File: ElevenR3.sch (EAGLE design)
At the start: 63 parts, among them IC1 ATMEGA328P, IC2 ATMEGA16U2-MU, IC3 MC33269DT-5.0, IC4 LM358D, IC5 LP2985-33DBVR, J2 Analog, J3 Digital_8_13, J4 Digital_0_7, J5 DC_2_1MM, J6 Digital_0_7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

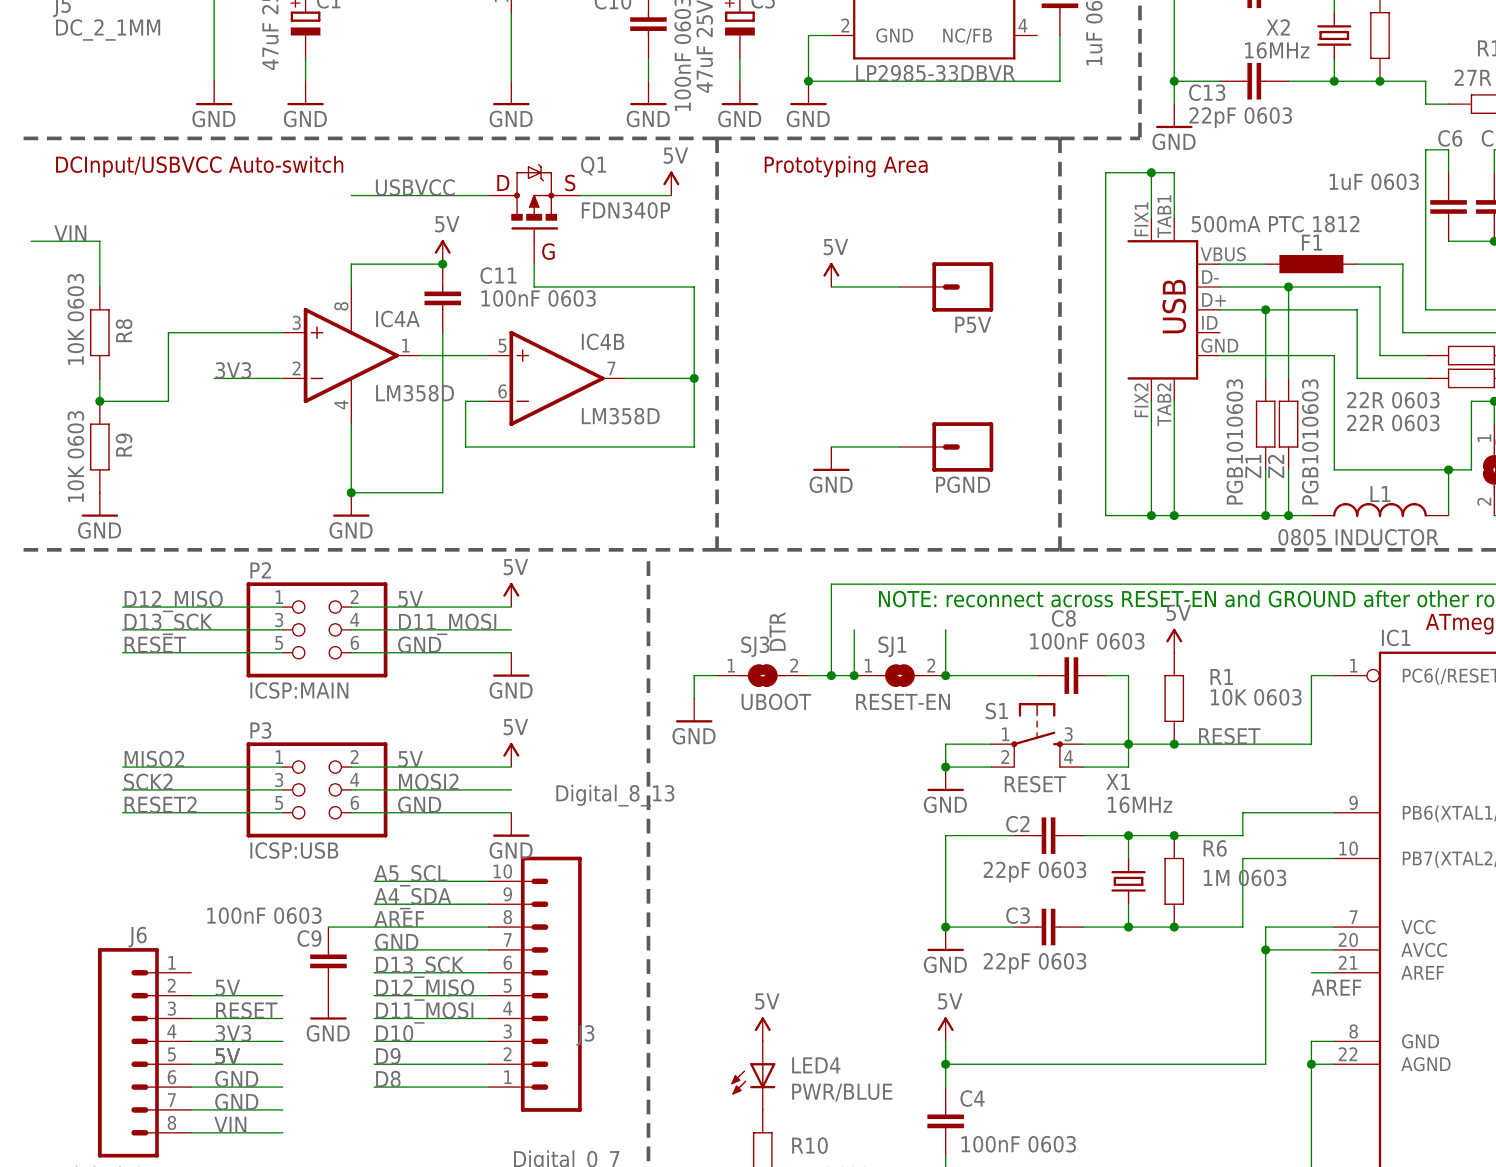
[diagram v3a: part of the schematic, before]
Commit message: Replaced uUSB footprint
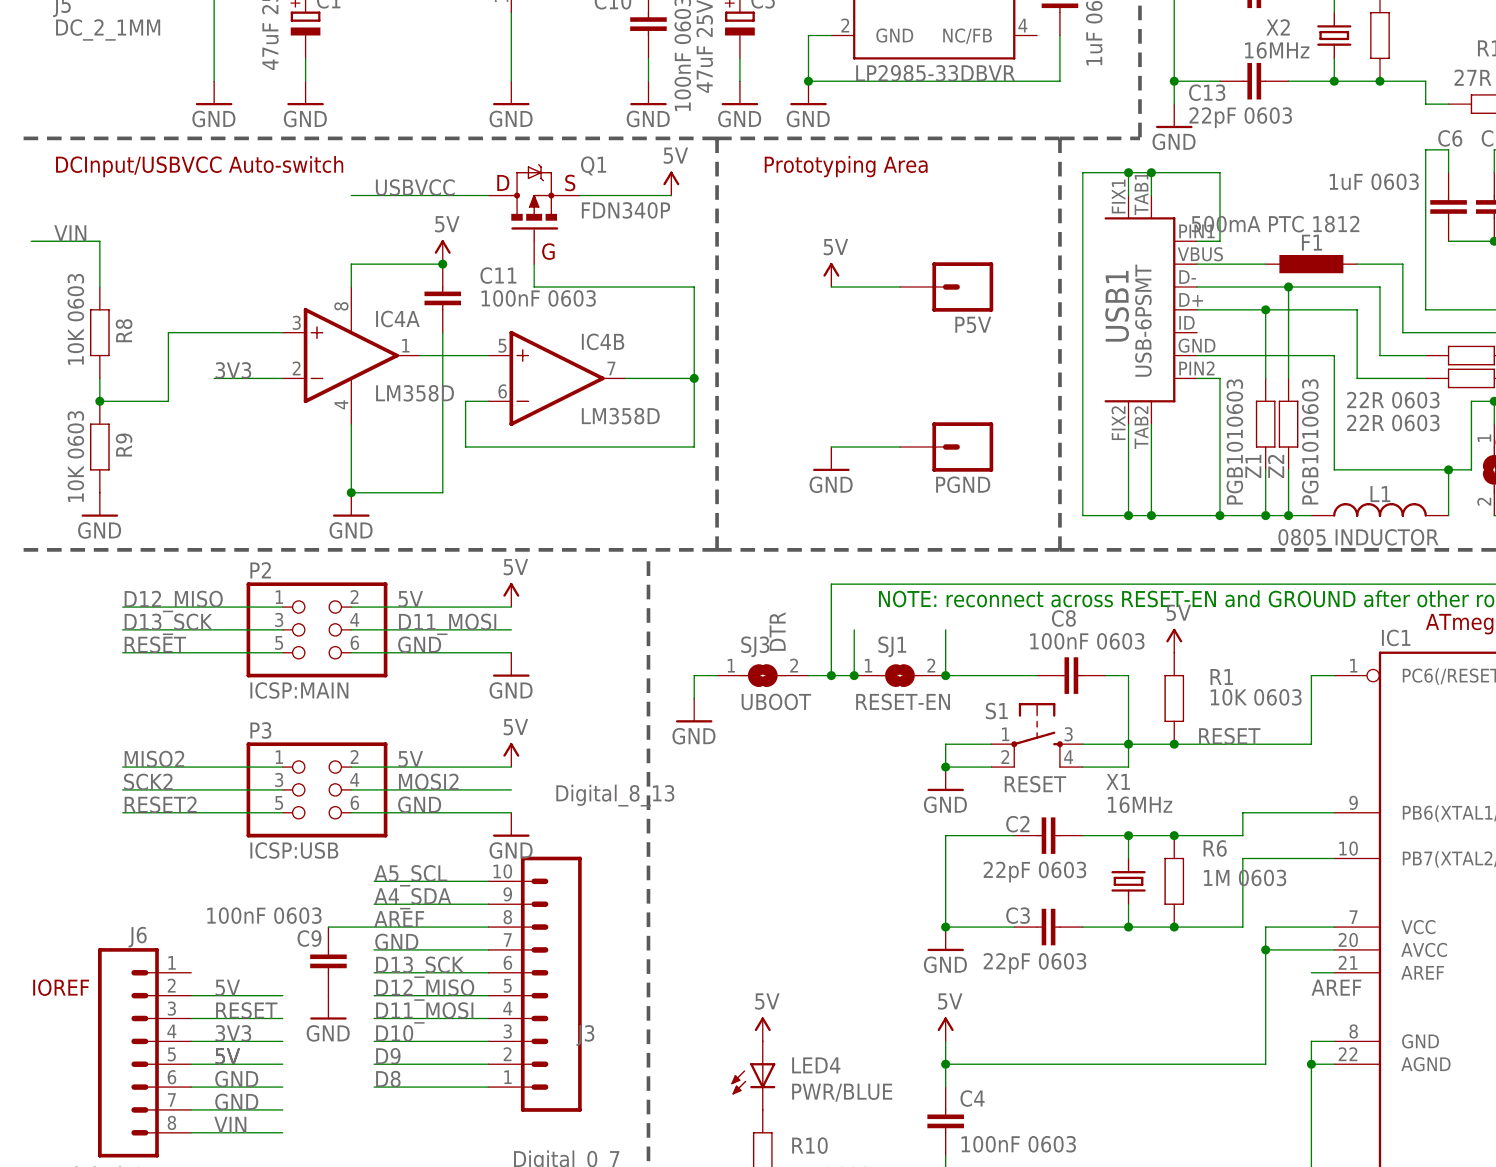
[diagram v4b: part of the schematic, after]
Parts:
- removed X3: USBSF-MICROB, freetronics-jon:USBSF-MICROB
- added USB1: USB-6PSMT, freetronics-jon:USB-6PSMT
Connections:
- net N$115: now also USB1.VBUS; no longer X3.VBUS
- net N$16: now also USB1.D+; no longer X3.D+
- net N$17: now also USB1.D-; no longer X3.D-
- net N$3: now also USB1.FIX1, USB1.FIX2, USB1.PIN1, USB1.PIN2, USB1.TAB1, USB1.TAB2; no longer X3.FIX1, X3.FIX2, X3.TAB1, X3.TAB2
- net UGND: now also USB1.GND; no longer X3.GND
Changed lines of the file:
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@@
 <part name="GND6" library="SparkFun" deviceset="GND" device=""/>
 <part name="J6" library="freetronics" deviceset="M08" device="" value="Digital_0_7"/>
-<part name="X3" library="freetronics-jon" deviceset="USBSF" device="-MICROB"/>
+<part name="USB1" library="freetronics-jon" deviceset="USB-6P" device="SMT"/>
 </parts>
 <sheets>
@@
 <frame x1="142.24" y1="5.08" x2="243.84" y2="17.78" columns="0" rows="0" layer="94" border-left="no" border-top="no" border-right="no" border-bottom="no"/>
 <text x="167.64" y="111.76" size="1.27" layer="94">(Linked)</text>
+<text x="5.08" y="50.8" size="1.778" layer="94">IOREF</text>
 </plain>
 <instances>
@@
 <attribute name="VALUE" x="8.128" y="31.75" size="1.778" layer="96" rot="MR180"/>
 </instance>
-<instance part="X3" gate="G$1" x="132.08" y="127" rot="R180"/>
+<instance part="USB1" gate="G$1" x="129.54" y="127" smashed="yes" rot="R180">
+<attribute name="NAME" x="127" y="123.19" size="2.54" layer="95" rot="R90"/>
+<attribute name="VALUE" x="129.54" y="119.38" size="1.778" layer="96" rot="R90"/>
+</instance>
 </instances>
 <busses>
@@
 <pinref part="Z2" gate="G$1" pin="2"/>
 <pinref part="L1" gate="G$1" pin="1"/>
-<pinref part="X3" gate="G$1" pin="TAB2"/>
-<wire x1="132.08" y1="116.84" x2="132.08" y2="104.14" width="0.1524" layer="91"/>
-<wire x1="132.08" y1="104.14" x2="142.24" y2="104.14" width="0.1524" layer="91"/>
-<pinref part="X3" gate="G$1" pin="TAB1"/>
-<wire x1="132.08" y1="137.16" x2="132.08" y2="142.24" width="0.1524" layer="91"/>
-<wire x1="132.08" y1="142.24" x2="129.54" y2="142.24" width="0.1524" layer="91"/>
-<wire x1="129.54" y1="142.24" x2="124.46" y2="142.24" width="0.1524" layer="91"/>
-<wire x1="124.46" y1="142.24" x2="124.46" y2="104.14" width="0.1524" layer="91"/>
-<wire x1="124.46" y1="104.14" x2="129.54" y2="104.14" width="0.1524" layer="91"/>
-<junction x="132.08" y="104.14"/>
-<pinref part="X3" gate="G$1" pin="FIX1"/>
-<wire x1="129.54" y1="104.14" x2="132.08" y2="104.14" width="0.1524" layer="91"/>
-<wire x1="129.54" y1="137.16" x2="129.54" y2="142.24" width="0.1524" layer="91"/>
-<pinref part="X3" gate="G$1" pin="FIX2"/>
-<wire x1="129.54" y1="116.84" x2="129.54" y2="104.14" width="0.1524" layer="91"/>
+<pinref part="USB1" gate="G$1" pin="TAB2"/>
+<wire x1="129.54" y1="114.3" x2="129.54" y2="104.14" width="0.1524" layer="91"/>
+<wire x1="129.54" y1="104.14" x2="137.16" y2="104.14" width="0.1524" layer="91"/>
+<pinref part="USB1" gate="G$1" pin="TAB1"/>
+<wire x1="137.16" y1="104.14" x2="142.24" y2="104.14" width="0.1524" layer="91"/>
+<wire x1="129.54" y1="139.7" x2="129.54" y2="142.24" width="0.1524" layer="91"/>
+<wire x1="129.54" y1="142.24" x2="127" y2="142.24" width="0.1524" layer="91"/>
+<wire x1="127" y1="142.24" x2="121.92" y2="142.24" width="0.1524" layer="91"/>
+<wire x1="121.92" y1="142.24" x2="121.92" y2="104.14" width="0.1524" layer="91"/>
+<wire x1="121.92" y1="104.14" x2="127" y2="104.14" width="0.1524" layer="91"/>
 <junction x="129.54" y="104.14"/>
+<pinref part="USB1" gate="G$1" pin="FIX1"/>
+<wire x1="127" y1="104.14" x2="129.54" y2="104.14" width="0.1524" layer="91"/>
+<wire x1="127" y1="139.7" x2="127" y2="142.24" width="0.1524" layer="91"/>
+<pinref part="USB1" gate="G$1" pin="FIX2"/>
+<wire x1="127" y1="114.3" x2="127" y2="104.14" width="0.1524" layer="91"/>
+<wire x1="129.54" y1="142.24" x2="137.16" y2="142.24" width="0.1524" layer="91"/>
+<wire x1="137.16" y1="142.24" x2="137.16" y2="134.62" width="0.1524" layer="91"/>
+<pinref part="USB1" gate="G$1" pin="PIN1"/>
+<wire x1="137.16" y1="134.62" x2="134.62" y2="134.62" width="0.1524" layer="91"/>
+<pinref part="USB1" gate="G$1" pin="PIN2"/>
+<wire x1="134.62" y1="119.38" x2="137.16" y2="119.38" width="0.1524" layer="91"/>
+<wire x1="137.16" y1="119.38" x2="137.16" y2="104.14" width="0.1524" layer="91"/>
+<junction x="127" y="104.14"/>
+<junction x="137.16" y="104.14"/>
 <junction x="129.54" y="142.24"/>
+<junction x="127" y="142.24"/>
 </segment>
 </net>
@@
 <pinref part="Z1" gate="G$1" pin="1"/>
 <pinref part="R15" gate="G$1" pin="2"/>
-<pinref part="X3" gate="G$1" pin="D+"/>
-<wire x1="142.24" y1="127" x2="137.16" y2="127" width="0.1524" layer="91"/>
+<pinref part="USB1" gate="G$1" pin="D+"/>
+<wire x1="142.24" y1="127" x2="134.62" y2="127" width="0.1524" layer="91"/>
 </segment>
 </net>
@@
 <pinref part="Z2" gate="G$1" pin="1"/>
 <pinref part="R14" gate="G$1" pin="2"/>
-<pinref part="X3" gate="G$1" pin="D-"/>
-<wire x1="137.16" y1="129.54" x2="144.78" y2="129.54" width="0.1524" layer="91"/>
+<pinref part="USB1" gate="G$1" pin="D-"/>
+<wire x1="134.62" y1="129.54" x2="144.78" y2="129.54" width="0.1524" layer="91"/>
 </segment>
 </net>
@@
 <segment>
 <pinref part="F1" gate="G$1" pin="1"/>
-<pinref part="X3" gate="G$1" pin="VBUS"/>
-<wire x1="142.24" y1="132.08" x2="137.16" y2="132.08" width="0.1524" layer="91"/>
+<pinref part="USB1" gate="G$1" pin="VBUS"/>
+<wire x1="142.24" y1="132.08" x2="134.62" y2="132.08" width="0.1524" layer="91"/>
 </segment>
 </net>
@@
 <net name="UGND" class="0">
 <segment>
-<wire x1="137.16" y1="121.92" x2="149.86" y2="121.92" width="0.1524" layer="91"/>
+<wire x1="134.62" y1="121.92" x2="149.86" y2="121.92" width="0.1524" layer="91"/>
 <wire x1="149.86" y1="121.92" x2="149.86" y2="109.22" width="0.1524" layer="91"/>
 <wire x1="149.86" y1="109.22" x2="162.56" y2="109.22" width="0.1524" layer="91"/>
@@
 <pinref part="IC2" gate="G$1" pin="UGND"/>
 <pinref part="SJ2" gate="1" pin="1"/>
-<pinref part="X3" gate="G$1" pin="GND"/>
+<pinref part="USB1" gate="G$1" pin="GND"/>
 <wire x1="170.18" y1="116.84" x2="170.18" y2="114.3" width="0.1524" layer="91"/>
 <junction x="170.18" y="116.84"/>

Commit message: Production release v2.0 after small revisions
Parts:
- J1: value Digital_0_7 -> Power
- LED1: value RX -> RX/GRN
- LED2: value TX -> TX/YEL
- renumbered J6 to J1, USB1 to P1
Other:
- note removed: "SCL/SDA"
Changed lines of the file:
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@@
 <part name="R2" library="freetronics" deviceset="RESISTOR" device="0603" value="1K 0603"/>
 <part name="R3" library="freetronics" deviceset="RESISTOR" device="0603" value="1K 0603"/>
-<part name="LED1" library="freetronics" deviceset="LED" device="0603" value="RX"/>
-<part name="LED2" library="freetronics" deviceset="LED" device="0603" value="TX"/>
+<part name="LED1" library="freetronics" deviceset="LED" device="0603" value="RX/GRN"/>
+<part name="LED2" library="freetronics" deviceset="LED" device="0603" value="TX/YEL"/>
 <part name="U$2" library="SparkFun" deviceset="5V" device=""/>
 <part name="R4" library="freetronics" deviceset="RESISTOR" device="0603" value="1K 0603"/>
@@
 <part name="GND1" library="SparkFun" deviceset="GND" device=""/>
 <part name="GND6" library="SparkFun" deviceset="GND" device=""/>
-<part name="J6" library="freetronics" deviceset="M08" device="" value="Digital_0_7"/>
-<part name="USB1" library="freetronics-jon" deviceset="USB-6P" device="SMT"/>
+<part name="J1" library="freetronics" deviceset="M08" device="" value="Power"/>
+<part name="P1" library="freetronics-jon" deviceset="USB-6P" device="SMT"/>
 </parts>
 <sheets>
@@
 <frame x1="0" y1="0" x2="248.92" y2="185.42" columns="8" rows="5" layer="94"/>
 <frame x1="83.82" y1="101.6" x2="116.84" y2="139.7" columns="0" rows="0" layer="94"/>
-<text x="254" y="160.02" size="1.778" layer="91">IOREF</text>
-<text x="254" y="154.94" size="1.778" layer="91">SCL/SDA</text>
 <text x="144.78" y="20.32" size="3.048" layer="94">Freetronics "Eleven" R3</text>
 <text x="170.18" y="14.478" size="1.778" layer="94">V3.0 (2012-07-02)</text>
@@
 <instance part="J3" gate="G$1" x="66.04" y="58.42" smashed="yes" rot="MR0">
 <attribute name="NAME" x="67.818" y="45.72" size="1.778" layer="95" rot="MR0"/>
-<attribute name="VALUE" x="76.708" y="72.39" size="1.778" layer="96" rot="MR0"/>
+<attribute name="VALUE" x="71.628" y="35.56" size="1.778" layer="96" rot="MR0"/>
 </instance>
 <instance part="J4" gate="G$1" x="60.96" y="17.78" smashed="yes" rot="MR0">
@@
 <instance part="F1" gate="G$1" x="147.32" y="132.08" smashed="yes" rot="R90">
 <attribute name="NAME" x="146.05" y="133.5786" size="1.778" layer="95"/>
-<attribute name="VALUE" x="133.858" y="135.636" size="1.778" layer="96"/>
+<attribute name="VALUE" x="138.938" y="135.636" size="1.778" layer="96"/>
 </instance>
 <instance part="R2" gate="G$1" x="241.3" y="129.54" smashed="yes" rot="R90">
@@
 <instance part="LED1" gate="G$1" x="241.3" y="142.24" smashed="yes">
 <attribute name="NAME" x="239.776" y="132.588" size="1.778" layer="95" rot="R90"/>
-<attribute name="VALUE" x="239.649" y="143.256" size="1.778" layer="96" rot="R90"/>
+<attribute name="VALUE" x="237.109" y="140.716" size="1.778" layer="96" rot="R90"/>
 </instance>
 <instance part="LED2" gate="G$1" x="233.68" y="142.24" smashed="yes">
 <attribute name="NAME" x="232.156" y="132.588" size="1.778" layer="95" rot="R90"/>
-<attribute name="VALUE" x="232.029" y="143.256" size="1.778" layer="96" rot="R90"/>
+<attribute name="VALUE" x="229.489" y="140.716" size="1.778" layer="96" rot="R90"/>
 </instance>
 <instance part="U$2" gate="G$1" x="241.3" y="147.32"/>
@@
 <attribute name="VALUE" x="180.34" y="101.6" size="1.778" layer="96"/>
 </instance>
-<instance part="J6" gate="G$1" x="17.78" y="45.72" smashed="yes" rot="MR180">
+<instance part="J1" gate="G$1" x="17.78" y="45.72" smashed="yes" rot="MR180">
 <attribute name="NAME" x="16.002" y="58.42" size="1.778" layer="95" rot="MR180"/>
-<attribute name="VALUE" x="8.128" y="31.75" size="1.778" layer="96" rot="MR180"/>
-</instance>
-<instance part="USB1" gate="G$1" x="129.54" y="127" smashed="yes" rot="R180">
+<attribute name="VALUE" x="12.446" y="32.004" size="1.778" layer="96" rot="MR180"/>
+</instance>
+<instance part="P1" gate="G$1" x="129.54" y="127" smashed="yes" rot="R180">
 <attribute name="NAME" x="127" y="123.19" size="2.54" layer="95" rot="R90"/>
 <attribute name="VALUE" x="129.54" y="119.38" size="1.778" layer="96" rot="R90"/>
@@
 <segment>
 <label x="25.4" y="45.72" size="1.778" layer="95"/>
-<pinref part="J6" gate="G$1" pin="4"/>
+<pinref part="J1" gate="G$1" pin="4"/>
 <wire x1="22.86" y1="45.72" x2="33.02" y2="45.72" width="0.1524" layer="91"/>
 </segment>
@@
 <label x="25.4" y="43.18" size="1.778" layer="95"/>
 <label x="25.4" y="43.18" size="1.778" layer="95"/>
-<pinref part="J6" gate="G$1" pin="5"/>
+<pinref part="J1" gate="G$1" pin="5"/>
 <wire x1="22.86" y1="43.18" x2="33.02" y2="43.18" width="0.1524" layer="91"/>
 </segment>
@@
 </segment>
 <segment>
-<pinref part="J6" gate="G$1" pin="2"/>
+<pinref part="J1" gate="G$1" pin="2"/>
 <wire x1="22.86" y1="50.8" x2="33.02" y2="50.8" width="0.1524" layer="91"/>
 <label x="25.4" y="50.8" size="1.778" layer="95"/>
@@
 <segment>
 <label x="25.4" y="40.64" size="1.778" layer="95"/>
-<pinref part="J6" gate="G$1" pin="6"/>
+<pinref part="J1" gate="G$1" pin="6"/>
 <wire x1="33.02" y1="40.64" x2="22.86" y2="40.64" width="0.1524" layer="91"/>
 </segment>
 <segment>
 <label x="25.4" y="38.1" size="1.778" layer="95"/>
-<pinref part="J6" gate="G$1" pin="7"/>
+<pinref part="J1" gate="G$1" pin="7"/>
 <wire x1="22.86" y1="38.1" x2="33.02" y2="38.1" width="0.1524" layer="91"/>
 </segment>
@@
 <segment>
 <label x="25.4" y="35.56" size="1.778" layer="95"/>
-<pinref part="J6" gate="G$1" pin="8"/>
+<pinref part="J1" gate="G$1" pin="8"/>
 <wire x1="33.02" y1="35.56" x2="22.86" y2="35.56" width="0.1524" layer="91"/>
 </segment>
@@
 <label x="134.62" y="78.74" size="1.778" layer="95"/>
 <label x="15.24" y="88.9" size="1.778" layer="95"/>
-<pinref part="J6" gate="G$1" pin="3"/>
+<pinref part="J1" gate="G$1" pin="3"/>
 <wire x1="33.02" y1="48.26" x2="22.86" y2="48.26" width="0.1524" layer="91"/>
 </segment>
@@
 <pinref part="Z2" gate="G$1" pin="2"/>
 <pinref part="L1" gate="G$1" pin="1"/>
-<pinref part="USB1" gate="G$1" pin="TAB2"/>
+<pinref part="P1" gate="G$1" pin="TAB2"/>
 <wire x1="129.54" y1="114.3" x2="129.54" y2="104.14" width="0.1524" layer="91"/>
 <wire x1="129.54" y1="104.14" x2="137.16" y2="104.14" width="0.1524" layer="91"/>
-<pinref part="USB1" gate="G$1" pin="TAB1"/>
+<pinref part="P1" gate="G$1" pin="TAB1"/>
 <wire x1="137.16" y1="104.14" x2="142.24" y2="104.14" width="0.1524" layer="91"/>
 <wire x1="129.54" y1="139.7" x2="129.54" y2="142.24" width="0.1524" layer="91"/>
@@
 <wire x1="121.92" y1="104.14" x2="127" y2="104.14" width="0.1524" layer="91"/>
 <junction x="129.54" y="104.14"/>
-<pinref part="USB1" gate="G$1" pin="FIX1"/>
+<pinref part="P1" gate="G$1" pin="FIX1"/>
 <wire x1="127" y1="104.14" x2="129.54" y2="104.14" width="0.1524" layer="91"/>
 <wire x1="127" y1="139.7" x2="127" y2="142.24" width="0.1524" layer="91"/>
-<pinref part="USB1" gate="G$1" pin="FIX2"/>
+<pinref part="P1" gate="G$1" pin="FIX2"/>
 <wire x1="127" y1="114.3" x2="127" y2="104.14" width="0.1524" layer="91"/>
 <wire x1="129.54" y1="142.24" x2="137.16" y2="142.24" width="0.1524" layer="91"/>
 <wire x1="137.16" y1="142.24" x2="137.16" y2="134.62" width="0.1524" layer="91"/>
-<pinref part="USB1" gate="G$1" pin="PIN1"/>
+<pinref part="P1" gate="G$1" pin="PIN1"/>
 <wire x1="137.16" y1="134.62" x2="134.62" y2="134.62" width="0.1524" layer="91"/>
-<pinref part="USB1" gate="G$1" pin="PIN2"/>
+<pinref part="P1" gate="G$1" pin="PIN2"/>
 <wire x1="134.62" y1="119.38" x2="137.16" y2="119.38" width="0.1524" layer="91"/>
 <wire x1="137.16" y1="119.38" x2="137.16" y2="104.14" width="0.1524" layer="91"/>
@@
 <pinref part="Z1" gate="G$1" pin="1"/>
 <pinref part="R15" gate="G$1" pin="2"/>
-<pinref part="USB1" gate="G$1" pin="D+"/>
+<pinref part="P1" gate="G$1" pin="D+"/>
 <wire x1="142.24" y1="127" x2="134.62" y2="127" width="0.1524" layer="91"/>
 </segment>
@@
 <pinref part="Z2" gate="G$1" pin="1"/>
 <pinref part="R14" gate="G$1" pin="2"/>
-<pinref part="USB1" gate="G$1" pin="D-"/>
+<pinref part="P1" gate="G$1" pin="D-"/>
 <wire x1="134.62" y1="129.54" x2="144.78" y2="129.54" width="0.1524" layer="91"/>
 </segment>
@@
 <segment>
 <pinref part="F1" gate="G$1" pin="1"/>
-<pinref part="USB1" gate="G$1" pin="VBUS"/>
+<pinref part="P1" gate="G$1" pin="VBUS"/>
 <wire x1="142.24" y1="132.08" x2="134.62" y2="132.08" width="0.1524" layer="91"/>
 </segment>
@@
 <pinref part="IC2" gate="G$1" pin="UGND"/>
 <pinref part="SJ2" gate="1" pin="1"/>
-<pinref part="USB1" gate="G$1" pin="GND"/>
+<pinref part="P1" gate="G$1" pin="GND"/>
 <wire x1="170.18" y1="116.84" x2="170.18" y2="114.3" width="0.1524" layer="91"/>
 <junction x="170.18" y="116.84"/>
